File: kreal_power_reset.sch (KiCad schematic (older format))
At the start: 43 parts, among them J201 5V Bypass, P201 ICSP, Q201 BSS138, U101 PIC32MX775F, U201 MC34063, U202 AP3417C, U204 MMBZ5226BTS-3.3v, Y201 10.0MHz, Y202 32.768kHz

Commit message: Fixed swapped USB N and P lanes in schematic. NOT fixed in layout yet.
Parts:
- Q201: symbol BSS138 -> BSS138-RESCUE-KReal
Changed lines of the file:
@@
 VBUS
 $Comp
-L BSS138 Q201
+L BSS138-RESCUE-KReal Q201
 U 1 1 58F16BCD
 P 8980 1645

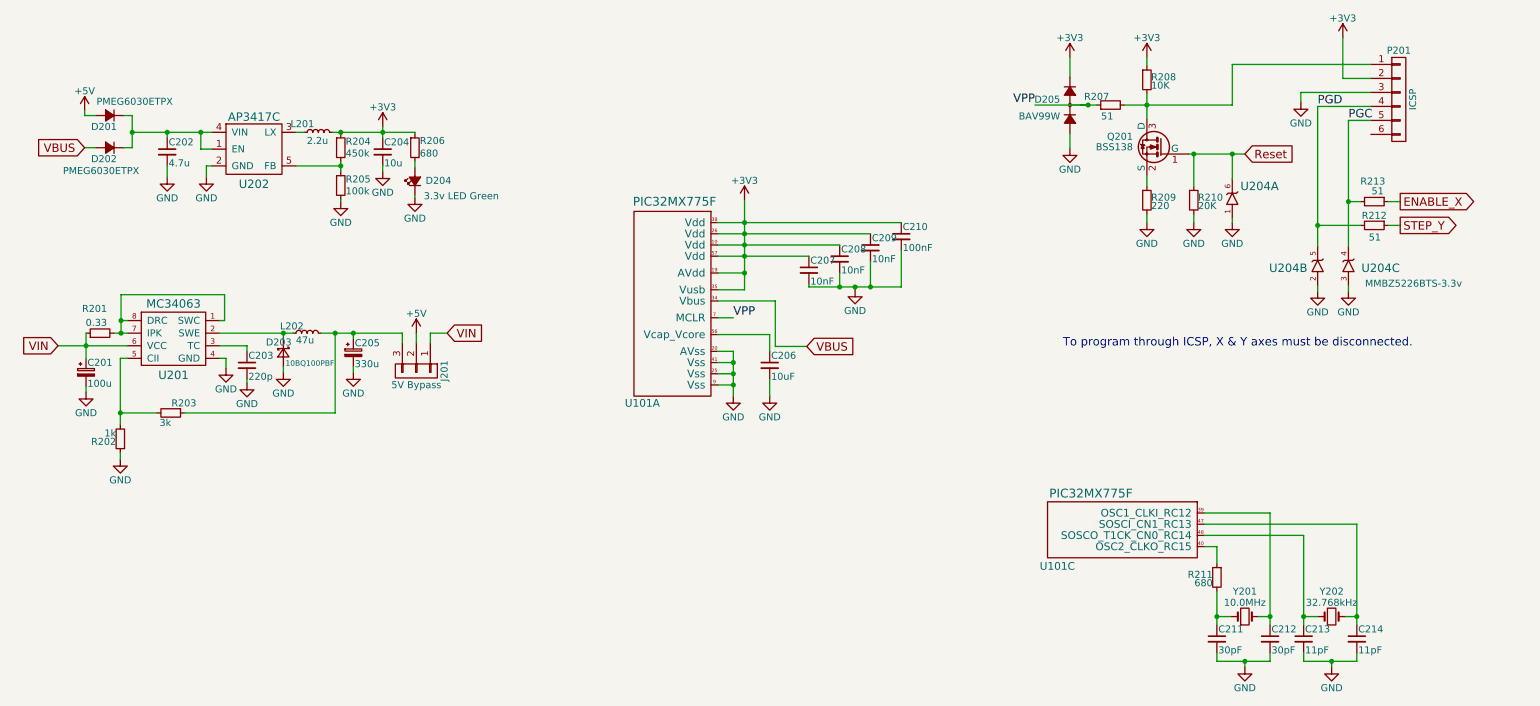
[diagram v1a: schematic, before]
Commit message: Fixed USB in layout. Fixed LEDs power source.
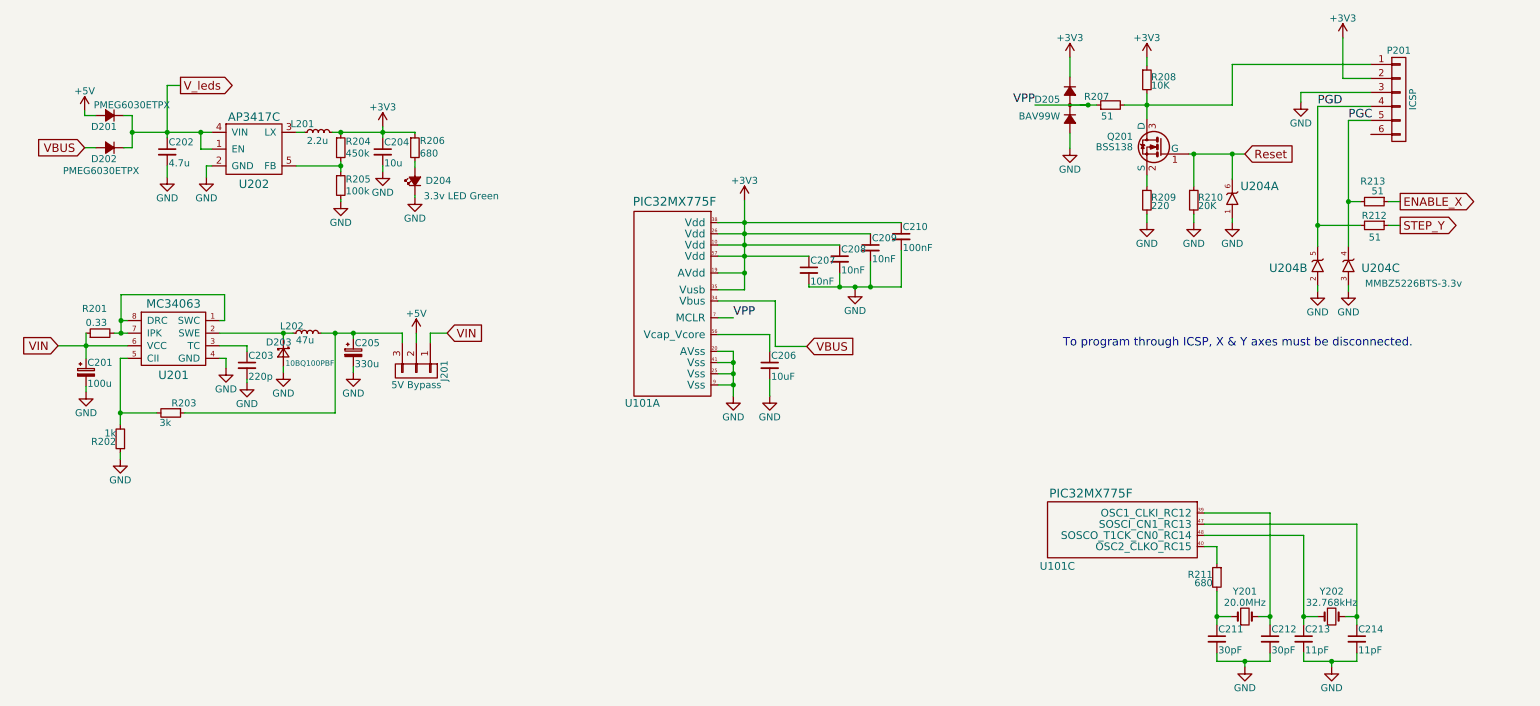
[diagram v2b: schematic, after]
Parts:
- Y201: value 10.0MHz -> 20.0MHz
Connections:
- net V_leds: now reaches C202.1, D201.1 (K), D202.1 (K), U202.1 (EN), U202.4 (VIN)
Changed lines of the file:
@@
 $EndComp
 $Comp
-L GND #PWR034
+L GND #PWR033
 U 1 1 58F15ABA
 P 6795 2665
-F 0 "#PWR034" H 6795 2415 50  0001 C CNN
+F 0 "#PWR033" H 6795 2415 50  0001 C CNN
 F 1 "GND" H 6795 2515 50  0000 C CNN
 F 2 "" H 6795 2665 50  0001 C CNN
@@
 $EndComp
 $Comp
-L GND #PWR035
+L GND #PWR034
 U 1 1 58F15ACE
 P 5925 3425
-F 0 "#PWR035" H 5925 3175 50  0001 C CNN
+F 0 "#PWR034" H 5925 3175 50  0001 C CNN
 F 1 "GND" H 5925 3275 50  0000 C CNN
 F 2 "" H 5925 3425 50  0001 C CNN
@@
 $EndComp
 $Comp
-L +3V3 #PWR036
+L +3V3 #PWR035
 U 1 1 58F15AD4
 P 6005 2025
-F 0 "#PWR036" H 6005 1875 50  0001 C CNN
+F 0 "#PWR035" H 6005 1875 50  0001 C CNN
 F 1 "+3V3" H 6005 2165 50  0000 C CNN
 F 2 "" H 6005 2025 50  0001 C CNN
@@
 $EndComp
 $Comp
-L GND #PWR037
+L GND #PWR036
 U 1 1 58F15B0A
 P 6185 3425
-F 0 "#PWR037" H 6185 3175 50  0001 C CNN
+F 0 "#PWR036" H 6185 3175 50  0001 C CNN
 F 1 "GND" H 6185 3275 50  0000 C CNN
 F 2 "" H 6185 3425 50  0001 C CNN
@@
 $EndComp
 $Comp
-L +3V3 #PWR038
+L +3V3 #PWR037
 U 1 1 58F16BDB
 P 10280 865
-F 0 "#PWR038" H 10280 715 50  0001 C CNN
+F 0 "#PWR037" H 10280 715 50  0001 C CNN
 F 1 "+3V3" H 10280 1005 50  0000 C CNN
 F 2 "" H 10280 865 50  0001 C CNN
@@
 $EndComp
 $Comp
-L GND #PWR039
+L GND #PWR038
 U 1 1 58F16BF9
 P 9980 1325
-F 0 "#PWR039" H 9980 1075 50  0001 C CNN
+F 0 "#PWR038" H 9980 1075 50  0001 C CNN
 F 1 "GND" H 9980 1175 50  0000 C CNN
 F 2 "" H 9980 1325 50  0001 C CNN
@@
 $EndComp
 $Comp
-L GND #PWR040
+L GND #PWR039
 U 1 1 58F16C1D
 P 8330 1655
-F 0 "#PWR040" H 8330 1405 50  0001 C CNN
+F 0 "#PWR039" H 8330 1405 50  0001 C CNN
 F 1 "GND" H 8330 1505 50  0000 C CNN
 F 2 "" H 8330 1655 50  0001 C CNN
@@
 $EndComp
 $Comp
-L GND #PWR041
+L GND #PWR040
 U 1 1 58F16C2D
 P 8880 2185
-F 0 "#PWR041" H 8880 1935 50  0001 C CNN
+F 0 "#PWR040" H 8880 1935 50  0001 C CNN
 F 1 "GND" H 8880 2035 50  0000 C CNN
 F 2 "" H 8880 2185 50  0001 C CNN
@@
 $EndComp
 $Comp
-L GND #PWR042
+L GND #PWR041
 U 1 1 58F16C33
 P 9215 2185
-F 0 "#PWR042" H 9215 1935 50  0001 C CNN
+F 0 "#PWR041" H 9215 1935 50  0001 C CNN
 F 1 "GND" H 9215 2035 50  0000 C CNN
 F 2 "" H 9215 2185 50  0001 C CNN
@@
 $EndComp
 $Comp
-L +3V3 #PWR043
+L +3V3 #PWR042
 U 1 1 58F16C3C
 P 8880 1005
-F 0 "#PWR043" H 8880 855 50  0001 C CNN
+F 0 "#PWR042" H 8880 855 50  0001 C CNN
 F 1 "+3V3" H 8880 1145 50  0000 C CNN
 F 2 "" H 8880 1005 50  0001 C CNN
@@
 $EndComp
 $Comp
-L +3V3 #PWR044
+L +3V3 #PWR043
 U 1 1 58F16C42
 P 8330 1005
-F 0 "#PWR044" H 8330 855 50  0001 C CNN
+F 0 "#PWR043" H 8330 855 50  0001 C CNN
 F 1 "+3V3" H 8330 1145 50  0000 C CNN
 F 2 "" H 8330 1005 50  0001 C CNN
@@
 $EndComp
 $Comp
-L GND #PWR045
+L GND #PWR044
 U 1 1 58F1920A
 P 9580 5360
-F 0 "#PWR045" H 9580 5110 50  0001 C CNN
+F 0 "#PWR044" H 9580 5110 50  0001 C CNN
 F 1 "GND" H 9580 5210 50  0000 C CNN
 F 2 "" H 9580 5360 50  0001 C CNN
@@
 $EndComp
 $Comp
-L GND #PWR046
+L GND #PWR045
 U 1 1 58F19237
 P 10200 5360
-F 0 "#PWR046" H 10200 5110 50  0001 C CNN
+F 0 "#PWR045" H 10200 5110 50  0001 C CNN
 F 1 "GND" H 10200 5210 50  0000 C CNN
 F 2 "" H 10200 5360 50  0001 C CNN
@@
 $EndComp
 $Comp
-L GND #PWR047
+L GND #PWR046
 U 1 1 58F23E2E
 P 2160 1860
-F 0 "#PWR047" H 2160 1610 50  0001 C CNN
+F 0 "#PWR046" H 2160 1610 50  0001 C CNN
 F 1 "GND" H 2160 1710 50  0000 C CNN
 F 2 "" H 2160 1860 50  0001 C CNN
@@
 $EndComp
 $Comp
-L +5V #PWR048
+L +5V #PWR047
 U 1 1 58F23EC6
 P 1290 1385
-F 0 "#PWR048" H 1290 1235 50  0001 C CNN
+F 0 "#PWR047" H 1290 1235 50  0001 C CNN
 F 1 "+5V" H 1290 1525 50  0000 C CNN
 F 2 "" H 1290 1385 50  0001 C CNN
@@
 $EndComp
 $Comp
-L GND #PWR049
+L GND #PWR048
 U 1 1 58F24A34
 P 3120 2035
-F 0 "#PWR049" H 3120 1785 50  0001 C CNN
+F 0 "#PWR048" H 3120 1785 50  0001 C CNN
 F 1 "GND" H 3120 1885 50  0000 C CNN
 F 2 "" H 3120 2035 50  0001 C CNN
@@
 $EndComp
 $Comp
-L GND #PWR050
+L GND #PWR049
 U 1 1 58F24A96
 P 1880 1860
-F 0 "#PWR050" H 1880 1610 50  0001 C CNN
+F 0 "#PWR049" H 1880 1610 50  0001 C CNN
 F 1 "GND" H 1880 1710 50  0000 C CNN
 F 2 "" H 1880 1860 50  0001 C CNN
@@
 $EndComp
 $Comp
-L GND #PWR051
+L GND #PWR050
 U 1 1 58F2501F
 P 3420 1820
-F 0 "#PWR051" H 3420 1570 50  0001 C CNN
+F 0 "#PWR050" H 3420 1570 50  0001 C CNN
 F 1 "GND" H 3420 1670 50  0000 C CNN
 F 2 "" H 3420 1820 50  0001 C CNN
@@
 $EndComp
 $Comp
-L +3V3 #PWR052
+L +3V3 #PWR051
 U 1 1 58F25A91
 P 3420 1500
-F 0 "#PWR052" H 3420 1350 50  0001 C CNN
+F 0 "#PWR051" H 3420 1350 50  0001 C CNN
 F 1 "+3V3" H 3420 1640 50  0000 C CNN
 F 2 "" H 3420 1500 50  0001 C CNN
@@
 $EndComp
 $Comp
-L GND #PWR053
+L GND #PWR052
 U 1 1 58F3856D
 P 9490 2185
-F 0 "#PWR053" H 9490 1935 50  0001 C CNN
+F 0 "#PWR052" H 9490 1935 50  0001 C CNN
 F 1 "GND" H 9490 2035 50  0000 C CNN
 F 2 "" H 9490 2185 50  0001 C CNN
@@
 $EndComp
 $Comp
-L GND #PWR054
+L GND #PWR053
 U 1 1 58F38678
 P 10100 2675
-F 0 "#PWR054" H 10100 2425 50  0001 C CNN
+F 0 "#PWR053" H 10100 2425 50  0001 C CNN
 F 1 "GND" H 10100 2525 50  0000 C CNN
 F 2 "" H 10100 2675 50  0001 C CNN
@@
 $EndComp
 $Comp
-L GND #PWR055
+L GND #PWR054
 U 1 1 58F386E3
 P 10320 2675
-F 0 "#PWR055" H 10320 2425 50  0001 C CNN
+F 0 "#PWR054" H 10320 2425 50  0001 C CNN
 F 1 "GND" H 10320 2525 50  0000 C CNN
 F 2 "" H 10320 2675 50  0001 C CNN
@@
 $EndComp
 $Comp
-L GND #PWR056
+L GND #PWR055
 U 1 1 58F3EF41
 P 3210 3255
-F 0 "#PWR056" H 3210 3005 50  0001 C CNN
+F 0 "#PWR055" H 3210 3005 50  0001 C CNN
 F 1 "GND" H 3210 3105 50  0000 C CNN
 F 2 "" H 3210 3255 50  0001 C CNN
@@
 $EndComp
 $Comp
-L GND #PWR057
+L GND #PWR056
 U 1 1 58F3F049
 P 2710 3255
-F 0 "#PWR057" H 2710 3005 50  0001 C CNN
+F 0 "#PWR056" H 2710 3005 50  0001 C CNN
 F 1 "GND" H 2710 3105 50  0000 C CNN
 F 2 "" H 2710 3255 50  0001 C CNN
@@
 $EndComp
 $Comp
-L GND #PWR058
+L GND #PWR057
 U 1 1 58F3F392
 P 2450 3330
-F 0 "#PWR058" H 2450 3080 50  0001 C CNN
+F 0 "#PWR057" H 2450 3080 50  0001 C CNN
 F 1 "GND" H 2450 3180 50  0000 C CNN
 F 2 "" H 2450 3330 50  0001 C CNN
@@
 $EndComp
 $Comp
-L GND #PWR059
+L GND #PWR058
 U 1 1 58F3F493
 P 2300 3225
-F 0 "#PWR059" H 2300 2975 50  0001 C CNN
+F 0 "#PWR058" H 2300 2975 50  0001 C CNN
 F 1 "GND" H 2300 3075 50  0000 C CNN
 F 2 "" H 2300 3225 50  0001 C CNN
@@
 $EndComp
 $Comp
-L GND #PWR060
+L GND #PWR059
 U 1 1 58F3F56B
 P 1545 3875
-F 0 "#PWR060" H 1545 3625 50  0001 C CNN
+F 0 "#PWR059" H 1545 3625 50  0001 C CNN
 F 1 "GND" H 1545 3725 50  0000 C CNN
 F 2 "" H 1545 3875 50  0001 C CNN
@@
 $EndComp
 $Comp
-L GND #PWR061
+L GND #PWR060
 U 1 1 58F3F79B
 P 1300 3395
-F 0 "#PWR061" H 1300 3145 50  0001 C CNN
+F 0 "#PWR060" H 1300 3145 50  0001 C CNN
 F 1 "GND" H 1300 3245 50  0000 C CNN
 F 2 "" H 1300 3395 50  0001 C CNN
@@
 VIN
 $Comp
-L +5V #PWR062
+L +5V #PWR061
 U 1 1 58F45216
 P 3660 2975
-F 0 "#PWR062" H 3660 2825 50  0001 C CNN
+F 0 "#PWR061" H 3660 2825 50  0001 C CNN
 F 1 "+5V" H 3660 3115 50  0000 C CNN
 F 2 "" H 3660 2975 50  0001 C CNN
@@
 P 1470 1420
 F 0 "D201" H 1420 1500 50  0000 L CNN
-F 1 "PMEG6030ETPX" H 1020 1320 50  0000 L CNN
+F 1 "PMEG6030ETPX" H 1040 1345 50  0000 L CNN
 F 2 "Diodes_SMD:D_SMA_Standard" V 1470 1420 50  0001 C CNN
 F 3 "" V 1470 1420 50  0001 C CNN
@@
 	1630 1650 1570 1650
 Wire Wire Line
-	1880 1580 1880 1540
-Wire Wire Line
 	1630 1420 1630 1650
-Wire Wire Line
-	1630 1540 2200 1540
-Connection ~ 2120 1540
 Connection ~ 1630 1540
-Connection ~ 1880 1540
 $Comp
 L R_Small R206
@@
 	3650 1750 3650 1790
 $Comp
-L GND #PWR063
+L GND #PWR062
 U 1 1 58F596CE
 P 3650 2005
-F 0 "#PWR063" H 3650 1755 50  0001 C CNN
+F 0 "#PWR062" H 3650 1755 50  0001 C CNN
 F 1 "GND" H 3650 1855 50  0000 C CNN
 F 2 "" H 3650 2005 50  0001 C CNN
@@
 P 9580 5000
 F 0 "Y201" H 9580 5180 50  0000 C CNN
-F 1 "10.0MHz" H 9580 5100 50  0000 C CNN
+F 1 "20.0MHz" H 9580 5100 50  0000 C CNN
 F 2 "Crystals:Crystal_SMD_0603-2pin_6.0x3.5mm" H 9580 5000 50  0001 C CNN
 F 3 "" H 9580 5000 50  0001 C CNN
@@
 Wire Wire Line
 	6005 2665 5815 2665
+Text GLabel 1975 1205 2    60   Output ~ 0
+V_leds
+Wire Wire Line
+	1975 1205 1880 1205
+Wire Wire Line
+	1630 1540 2200 1540
+Wire Wire Line
+	1880 1205 1880 1580
+Connection ~ 1880 1540
+Connection ~ 2120 1540
 $EndSCHEMATC
